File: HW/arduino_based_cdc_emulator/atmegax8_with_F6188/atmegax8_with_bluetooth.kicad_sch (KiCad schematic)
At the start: 75 parts, among them IC1 ATMEGA88-A, J1 Ant, J2 TMS, J3 TCK, J4 TDO, J5 TDI, P1 CONN_10, P2 SPI, P3 CONN_4, P4 SERIAL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

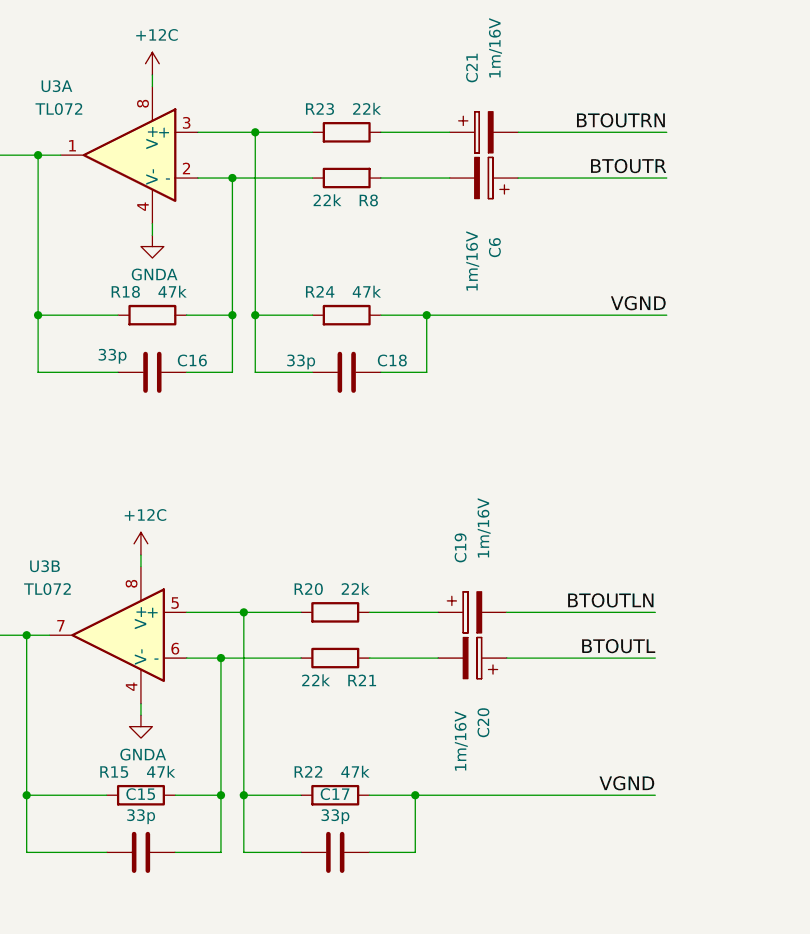
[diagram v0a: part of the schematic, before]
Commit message: fixes in HW for F6188
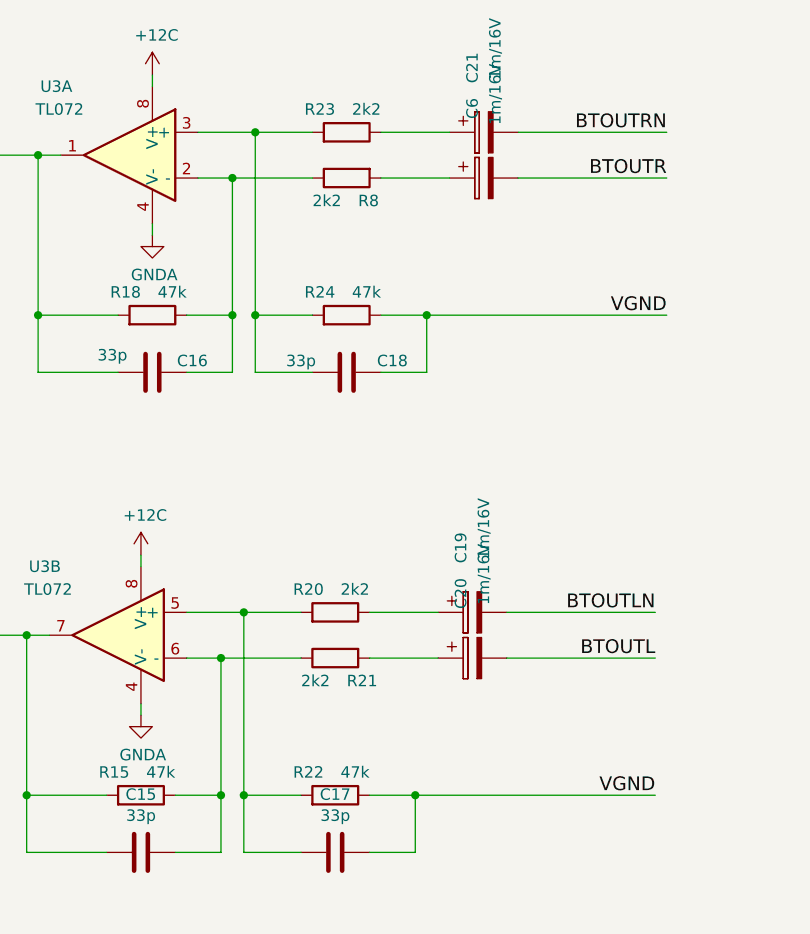
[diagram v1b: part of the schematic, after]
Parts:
- R20, R21, R23, R8: value 22k -> 2k2
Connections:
- net BTOUTL: now also C20.2; no longer C20.1
- net BTOUTR: now also C6.2; no longer C6.1
- net at R8.2: now also C6.1; no longer C6.2
- net at R21.2: now also C20.1; no longer C20.2
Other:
- moved on the sheet: C20, C6
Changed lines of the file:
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@@
   (junction (at 387.223 167.005))
   (no_connect (at 74.93 179.07))
+  (no_connect (at 74.93 166.37))
   (no_connect (at 74.93 219.71))
+  (no_connect (at 74.93 176.53))
   (no_connect (at 74.93 214.63))
+  (no_connect (at 74.93 187.96))
+  (no_connect (at 74.93 217.17))
   (no_connect (at 74.93 193.04))
+  (no_connect (at 74.93 195.58))
+  (no_connect (at 26.67 198.12))
   (no_connect (at 74.93 182.88))
-  (no_connect (at 74.93 176.53))
   (no_connect (at 26.67 195.58))
+  (no_connect (at 74.93 185.42))
   (no_connect (at 74.93 163.83))
-  (no_connect (at 74.93 166.37))
-  (no_connect (at 74.93 187.96))
-  (no_connect (at 26.67 198.12))
-  (no_connect (at 74.93 195.58))
-  (no_connect (at 74.93 185.42))
-  (no_connect (at 74.93 217.17))
   (wire (pts (xy 20.32 161.29) (xy 25.4 161.29))
     (stroke (width 0) (type solid) (color 0 0 0 0))
@@
       (effects (font (size 1.27 1.27)) (justify right))
     )
-    (property "Value" "22k" (id 1) (at 100.965 83.82 90)
+    (property "Value" "2k2" (id 1) (at 100.965 83.82 90)
       (effects (font (size 1.27 1.27)) (justify right))
     )
@@
       (effects (font (size 1.27 1.27)) (justify right))
     )
-    (property "Value" "22k" (id 1) (at 93.345 93.98 90)
+    (property "Value" "2k2" (id 1) (at 93.345 93.98 90)
       (effects (font (size 1.27 1.27)) (justify right))
     )
@@
       (effects (font (size 1.27 1.27)) (justify right))
     )
-    (property "Value" "22k" (id 1) (at 102.235 30.48 90)
+    (property "Value" "2k2" (id 1) (at 102.235 30.48 90)
       (effects (font (size 1.27 1.27)) (justify right))
     )
@@
       (effects (font (size 1.27 1.27)) (justify right))
     )
-    (property "Value" "22k" (id 1) (at 94.615 40.64 90)
+    (property "Value" "2k2" (id 1) (at 94.615 40.64 90)
       (effects (font (size 1.27 1.27)) (justify right))
     )
@@
     )
   )
-  (symbol (lib_id "atmegax8_with_bluetooth-rescue:CP-RESCUE-atmegax8_with_bluetooth") (at 112.395 91.44 270) (mirror x) (unit 1)
-    (in_bom yes)
-    (property "Reference" "C20" (id 0) (at 113.665 100.33 0)
-      (effects (font (size 1.27 1.27)) (justify left))
-    )
-    (property "Value" "1m/16V" (id 1) (at 111.125 104.14 0)
+  (symbol (lib_id "atmegax8_with_bluetooth-rescue:CP-RESCUE-atmegax8_with_bluetooth") (at 112.395 91.44 90) (mirror x) (unit 1)
+    (in_bom yes)
+    (property "Reference" "C20" (id 0) (at 111.125 82.55 0)
+      (effects (font (size 1.27 1.27)) (justify left))
+    )
+    (property "Value" "1m/16V" (id 1) (at 113.665 78.74 0)
       (effects (font (size 1.27 1.27)) (justify left))
     )
@@
     )
   )
-  (symbol (lib_id "atmegax8_with_bluetooth-rescue:CP-RESCUE-atmegax8_with_bluetooth") (at 113.665 38.1 270) (mirror x) (unit 1)
-    (in_bom yes)
-    (property "Reference" "C6" (id 0) (at 114.935 46.99 0)
-      (effects (font (size 1.27 1.27)) (justify left))
-    )
-    (property "Value" "1m/16V" (id 1) (at 112.395 50.8 0)
-      (effects (font (size 1.27 1.27)) (justify left))
-    )
+  (symbol (lib_id "atmegax8_with_bluetooth-rescue:CP-RESCUE-atmegax8_with_bluetooth") (at 113.665 38.1 90) (mirror x) (unit 1)
+    (in_bom yes)
+    (property "Reference" "C6" (id 0) (at 112.395 29.21 0)
+      (effects (font (size 1.27 1.27)) (justify left))
+    )
+    (property "Value" "1m/16V" (id 1) (at 114.935 25.4 0)
+      (effects (font (size 1.27 1.27)) (justify left))
+    )

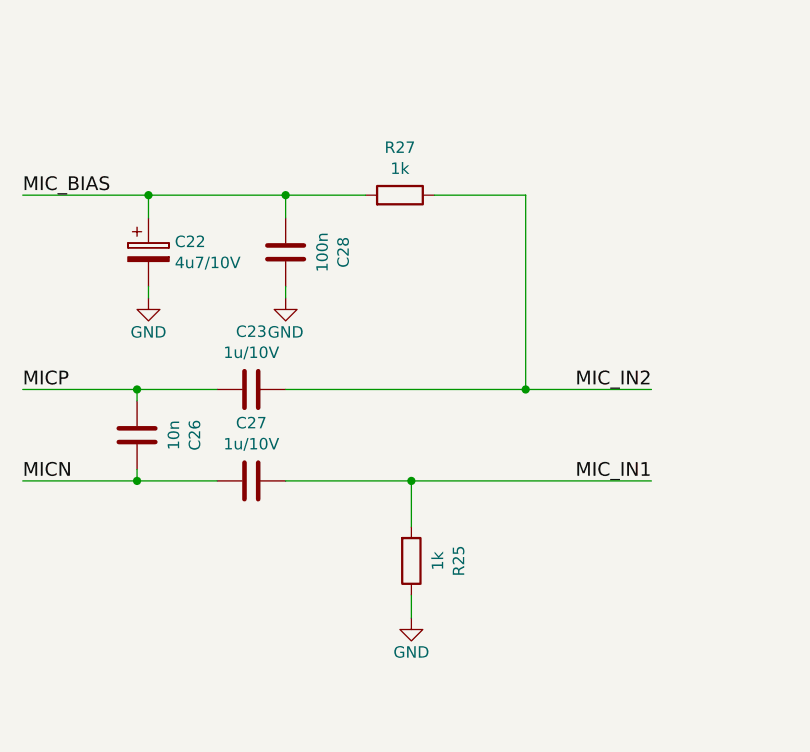
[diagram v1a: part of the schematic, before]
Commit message: correct value for mic resistors
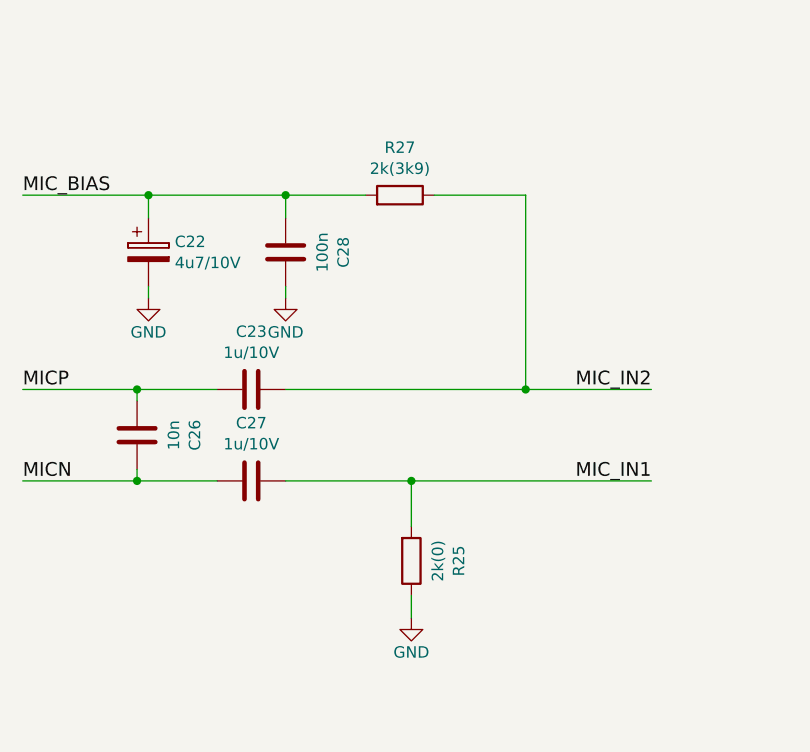
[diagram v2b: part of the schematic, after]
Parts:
- R25: value 1k -> 2k(0)
- R27: value 1k -> 2k(3k9)
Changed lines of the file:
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@@
   (junction (at 371.983 167.005))
   (junction (at 387.223 167.005))
-  (no_connect (at 74.93 179.07))
+  (no_connect (at 74.93 195.58))
+  (no_connect (at 74.93 219.71))
   (no_connect (at 74.93 166.37))
-  (no_connect (at 74.93 219.71))
-  (no_connect (at 74.93 176.53))
-  (no_connect (at 74.93 214.63))
+  (no_connect (at 74.93 185.42))
+  (no_connect (at 26.67 198.12))
   (no_connect (at 74.93 187.96))
   (no_connect (at 74.93 217.17))
   (no_connect (at 74.93 193.04))
-  (no_connect (at 74.93 195.58))
-  (no_connect (at 26.67 198.12))
   (no_connect (at 74.93 182.88))
+  (no_connect (at 74.93 176.53))
+  (no_connect (at 74.93 214.63))
+  (no_connect (at 74.93 163.83))
   (no_connect (at 26.67 195.58))
-  (no_connect (at 74.93 185.42))
-  (no_connect (at 74.93 163.83))
+  (no_connect (at 74.93 179.07))
   (wire (pts (xy 20.32 161.29) (xy 25.4 161.29))
     (stroke (width 0) (type solid) (color 0 0 0 0))
@@
     (in_bom yes)
     (property "Reference" "R27" (id 0) (at 233.045 34.7218 90))
-    (property "Value" "1k" (id 1) (at 233.045 37.059 90))
+    (property "Value" "2k(3k9)" (id 1) (at 233.045 37.059 90))
     (property "Footprint" "Resistors_SMD:R_0805_HandSoldering" (id 2) (at 233.045 40.005 0)
       (effects (font (size 1.524 1.524)) hide)
@@
     (in_bom yes)
     (property "Reference" "R25" (id 0) (at 239.5982 80.645 90))
-    (property "Value" "1k" (id 1) (at 237.2614 80.645 90))
+    (property "Value" "2k(0)" (id 1) (at 237.261 80.645 90))
     (property "Footprint" "Resistors_SMD:R_0805_HandSoldering" (id 2) (at 234.315 80.645 0)
       (effects (font (size 1.524 1.524)) hide)
